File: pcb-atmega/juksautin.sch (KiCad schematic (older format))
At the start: 29 parts, among them J1 Screw_Terminal_01x09, J2 Power out, J3 USB_C_Receptacle_USB2.0, J4 TagConnect, J5 EXTRA, J6 AREF_OUT, U1 SP3485EN, U2 SRV05-4, U3 R-78E5.0-0.5, U4 ATmega32U4-AU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

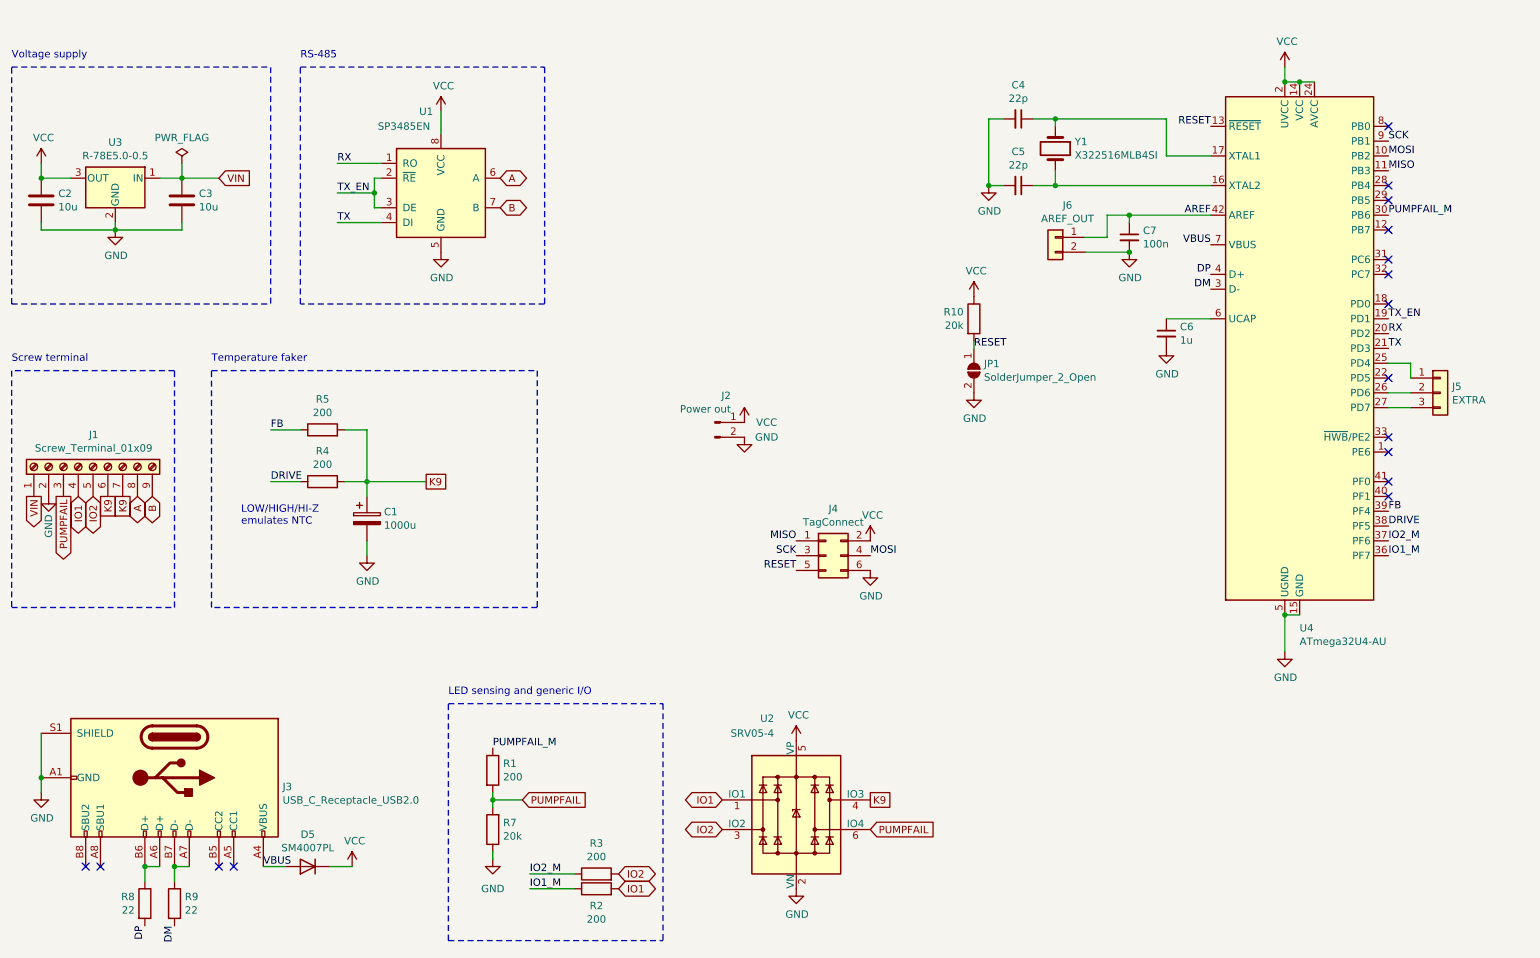
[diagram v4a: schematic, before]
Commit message: Atmega328 based pcb layed out
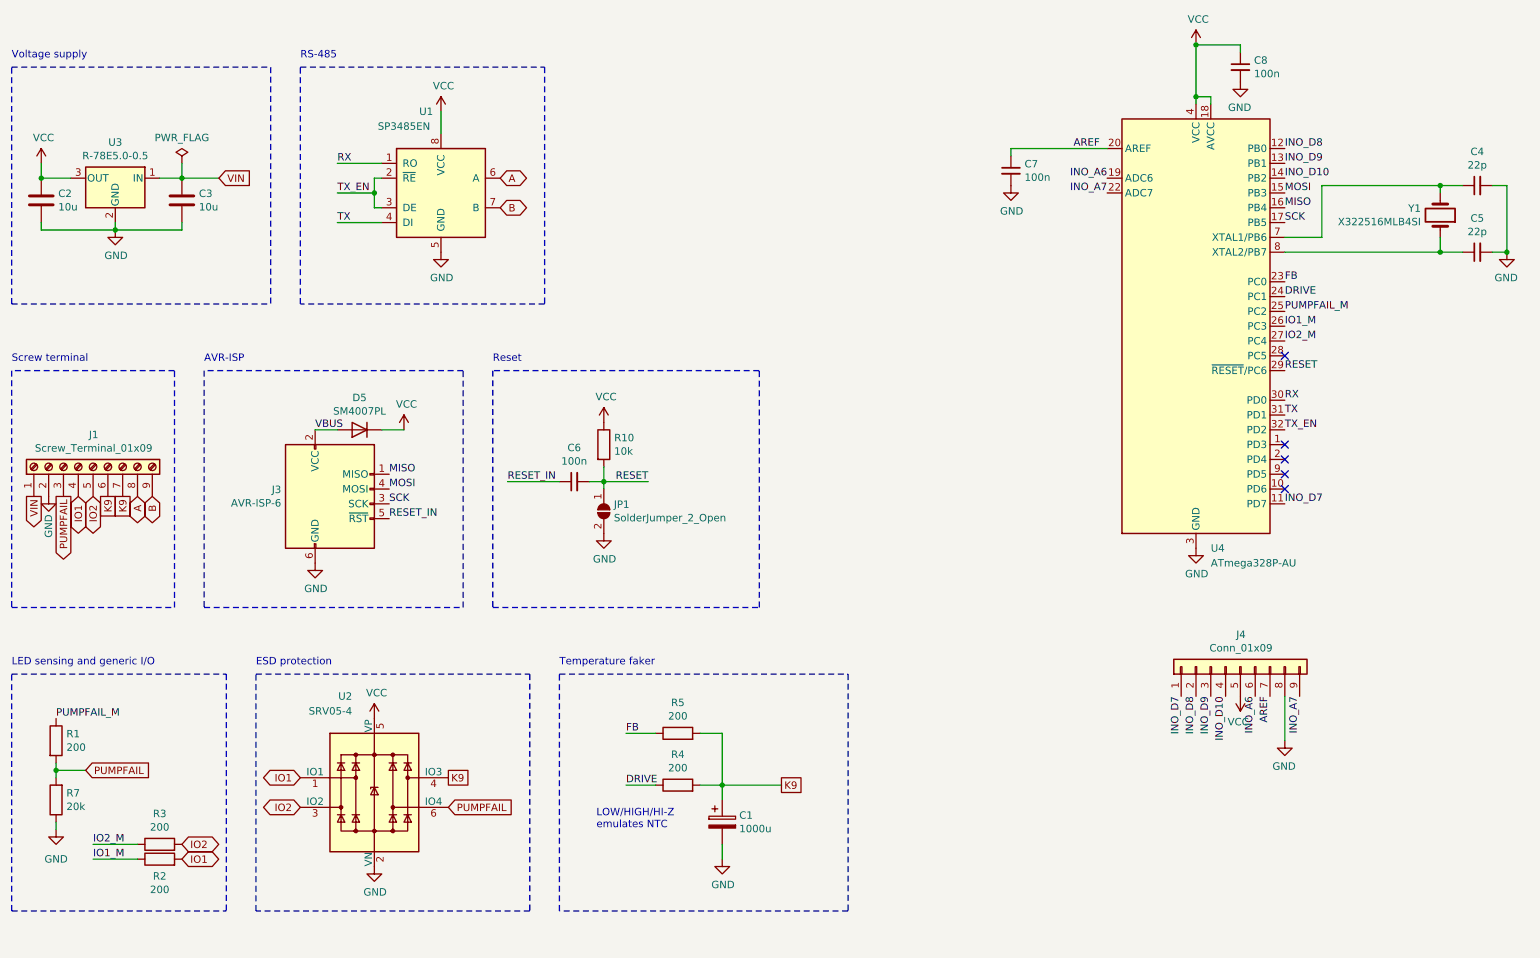
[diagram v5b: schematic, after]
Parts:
- removed J2: Power out, Connector_PinHeader_2.54mm:PinHeader_1x02_P2.54mm_Vertical, symbol Connector:Conn_01x02_Male
- removed J3: USB_C_Receptacle_USB2.0, Connector_USB:USB_C_Receptacle_HRO_TYPE-C-31-M-12, symbol Connector:USB_C_Receptacle_USB2.0
- removed J4: TagConnect, Connector:Tag-Connect_TC2030-IDC-NL_2x03_P1.27mm_Vertical, symbol Connector_Generic:Conn_02x03_Odd_Even
- removed J5: EXTRA, Connector_PinHeader_2.54mm:PinHeader_1x03_P2.54mm_Vertical, symbol Connector_Generic:Conn_01x03
- removed J6: AREF_OUT, Connector_PinHeader_2.54mm:PinHeader_1x02_P2.54mm_Vertical, symbol Connector_Generic:Conn_01x02
- removed R8, R9: 22, Resistor_SMD:R_0603_1608Metric, symbol Device:R
- removed U4: ATmega32U4-AU, Package_QFP:TQFP-44_10x10mm_P0.8mm, symbol MCU_Microchip_ATmega:ATmega32U4-AU
- added C8: 100n, Capacitor_SMD:C_0402_1005Metric, symbol Device:C_Small
- added J3: AVR-ISP-6, Connector_IDC:IDC-Header_2x03_P2.54mm_Horizontal, symbol Connector:AVR-ISP-6
- added J4: Conn_01x09, Connector_PinHeader_2.54mm:PinHeader_1x09_P2.54mm_Vertical, symbol Connector_Generic:Conn_01x09
- added U4: ATmega328P-AU, Package_QFP:TQFP-32_7x7mm_P0.8mm, symbol MCU_Microchip_ATmega:ATmega328P-AU
- C6: value 1u -> 100n; LCSC C52923 -> C1525
- R10: value 20k -> 10k; LCSC C4184 -> C25804
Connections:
- net AREF: now also J4.7 (Pin_7), U4.20 (AREF)
- net DRIVE: now also U4.24 (PC1)
- net FB: now also U4.23 (PC0)
- net GND: now also C8.2, J3.6 (GND), J4.8 (Pin_8), U4.21 (GND), U4.3 (GND), U4.5 (GND); no longer C6.2
- net IO1_M: now also U4.26 (PC3)
- net IO2_M: now also U4.27 (PC4)
- net MISO: now also J3.1 (MISO), U4.16 (PB4)
- net MOSI: now also J3.4 (MOSI), U4.15 (PB3)
- net PUMPFAIL_M: now also U4.25 (PC2)
- net RESET: now also C6.2, U4.29 (~RESET~/PC6)
- net RX: now also U4.30 (PD0)
- net SCK: now also J3.3 (SCK), U4.17 (PB5)
- net TX: now also U4.31 (PD1)
- net TX_EN: now also U4.32 (PD2)
- net VBUS: now also J3.2 (VCC)
- net VCC: now also C8.1, J4.5 (Pin_5), U4.18 (AVCC), U4.4 (VCC), U4.6 (VCC)
- net at C5.1: now also Y1.1, U4.8 (XTAL2/PB7); no longer Y1.2
- net at C4.1: now also Y1.2, U4.7 (XTAL1/PB6); no longer Y1.1
- net RESET_IN: now reaches C6.1
- net RESET_IN: now also J3.5 (~RST)
- new net INO_A6: J4.6 (Pin_6), U4.19 (ADC6)
- new net INO_A7: J4.9 (Pin_9), U4.22 (ADC7)
- new net INO_D10: J4.4 (Pin_4), U4.14 (PB2)
- new net INO_D7: J4.1 (Pin_1), U4.11 (PD7)
- new net INO_D8: J4.2 (Pin_2), U4.12 (PB0)
- new net INO_D9: J4.3 (Pin_3), U4.13 (PB1)
- no-connect marks 16 -> 5
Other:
- note added: "AVR-ISP"
- note added: "ESD protection"
- note added: "Reset"
- moved on the sheet: C1, C4, C5, C7, D5, JP1, R1, R10, R2, R3, R4, R5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

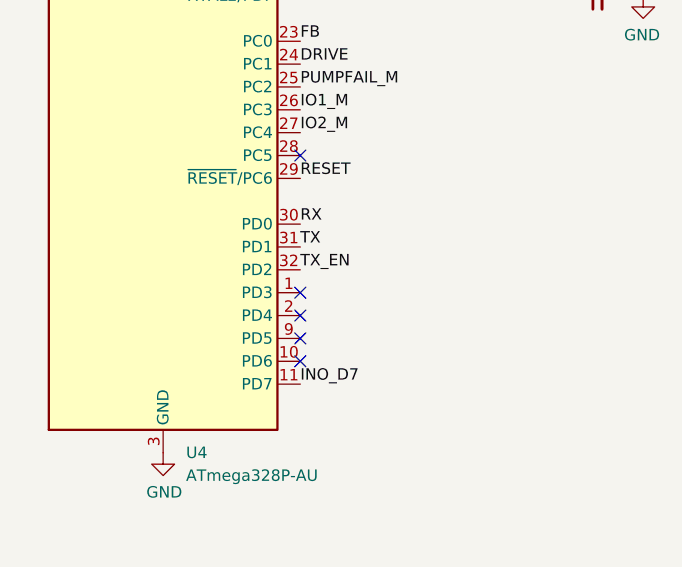
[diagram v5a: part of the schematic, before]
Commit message: Add an indicator LED
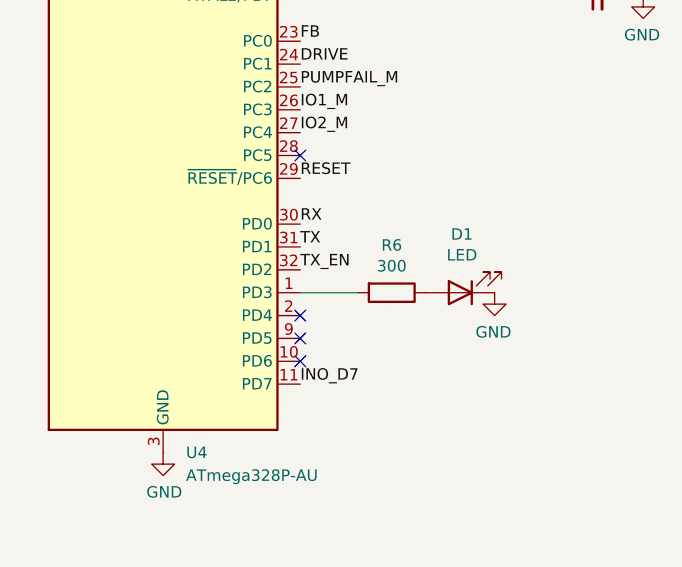
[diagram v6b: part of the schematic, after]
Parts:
- added D1: LED, LED_SMD:LED_0603_1608Metric, symbol Device:LED
- added R6: 300, Resistor_SMD:R_0603_1608Metric, symbol Device:R
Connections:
- net GND: now also D1.1 (K)
- net at U4.1 (PD3): now also R6.2
- new net: D1.2 (A), R6.1
- no-connect marks 5 -> 4
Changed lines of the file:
@@
 	0    -1   1    0
 $EndComp
-Connection ~ 10950 2250
 Wire Wire Line
 	10950 1800 10950 2250
@@
 L power:GND #PWR02
 U 1 1 60B9E570
-P 10950 2250
-F 0 "#PWR02" H 10950 2000 50  0001 C CNN
-F 1 "GND" H 10955 2077 50  0000 C CNN
-F 2 "" H 10950 2250 50  0001 C CNN
-F 3 "" H 10950 2250 50  0001 C CNN
-	1    10950 2250
+P 10300 3550
+F 0 "#PWR02" H 10300 3300 50  0001 C CNN
+F 1 "GND" H 10305 3377 50  0000 C CNN
+F 2 "" H 10300 3550 50  0001 C CNN
+F 3 "" H 10300 3550 50  0001 C CNN
+	1    10300 3550
 	-1   0    0    -1
 $EndComp
@@
 NoConn ~ 9450 2950
 NoConn ~ 9450 3850
-NoConn ~ 9450 3550
 Wire Wire Line
 	10500 1800 9700 1800
@@
 Text Label 9450 3950 0    50   ~ 0
 INO_D7
+$Comp
+L Device:LED D1
+U 1 1 61105A7E
+P 10150 3550
+F 0 "D1" H 10143 3295 50  0000 C CNN
+F 1 "LED" H 10143 3386 50  0000 C CNN
+F 2 "LED_SMD:LED_0603_1608Metric" H 10150 3550 50  0001 C CNN
+F 3 "~" H 10150 3550 50  0001 C CNN
+F 4 "C72043" H 10150 3550 50  0001 C CNN "LCSC"
+	1    10150 3550
+	-1   0    0    1
+$EndComp
+$Comp
+L Device:R R6
+U 1 1 611065FB
+P 9850 3550
+F 0 "R6" V 9643 3550 50  0000 C CNN
+F 1 "300" V 9734 3550 50  0000 C CNN
+F 2 "Resistor_SMD:R_0603_1608Metric" V 9780 3550 50  0001 C CNN
+F 3 "~" H 9850 3550 50  0001 C CNN
+F 4 "C23025" V 9850 3550 50  0001 C CNN "LCSC"
+	1    9850 3550
+	0    1    1    0
+$EndComp
+Wire Wire Line
+	9450 3550 9700 3550
+$Comp
+L power:GND #PWR?
+U 1 1 6111F566
+P 10950 2250
+F 0 "#PWR?" H 10950 2000 50  0001 C CNN
+F 1 "GND" H 10955 2077 50  0000 C CNN
+F 2 "" H 10950 2250 50  0001 C CNN
+F 3 "" H 10950 2250 50  0001 C CNN
+	1    10950 2250
+	-1   0    0    -1
+$EndComp
+Connection ~ 10950 2250
 $EndSCHEMATC

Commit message: pcb: Replace IDC-6 connector with plain pins. The casing is 3D printed.
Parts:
- J3: footprint Connector_IDC:IDC-Header_2x03_P2.54mm_Horizontal -> Connector_PinHeader_2.54mm:PinHeader_2x03_P2.54mm_Horizontal
- JP1: value SolderJumper_2_Open -> Reset pad
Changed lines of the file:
@@
 P 4850 4000
 F 0 "JP1" V 4804 4068 50  0000 L CNN
-F 1 "SolderJumper_2_Open" V 4895 4068 50  0000 L CNN
+F 1 "Reset pad" V 4895 4068 50  0000 L CNN
 F 2 "Jumper:SolderJumper-2_P1.3mm_Open_Pad1.0x1.5mm" H 4850 4000 50  0001 C CNN
 F 3 "~" H 4850 4000 50  0001 C CNN
@@
 F 0 "J3" H 2671 4046 50  0000 R CNN
 F 1 "AVR-ISP-6" H 2671 3955 50  0000 R CNN
-F 2 "Connector_IDC:IDC-Header_2x03_P2.54mm_Horizontal" V 2750 4000 50  0001 C CNN
+F 2 "Connector_PinHeader_2.54mm:PinHeader_2x03_P2.54mm_Horizontal" V 2750 4000 50  0001 C CNN
 F 3 " ~" H 1725 3400 50  0001 C CNN
 	1    3000 3950
@@
 	9450 3550 9700 3550
 $Comp
-L power:GND #PWR?
+L power:GND #PWR0106
 U 1 1 6111F566
 P 10950 2250
-F 0 "#PWR?" H 10950 2000 50  0001 C CNN
+F 0 "#PWR0106" H 10950 2000 50  0001 C CNN
 F 1 "GND" H 10955 2077 50  0000 C CNN
 F 2 "" H 10950 2250 50  0001 C CNN

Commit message: Schema and layout fixes after v0.9
- Crystal Y1 symbol changed to 4-pin, affecting the wiring as well
- Remove DC block capacitor C6, blocked RESET signal
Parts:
- removed C6: 100n, Capacitor_SMD:C_0402_1005Metric, symbol Device:C_Small
- removed Y1: X322516MLB4SI, Crystal:Crystal_SMD_3225-4Pin_3.2x2.5mm, symbol Device:Crystal
- added Y1: X322516MLB4SI, Crystal:Crystal_SMD_3225-4Pin_3.2x2.5mm, symbol Device:Crystal_GND24
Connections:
- net RESET_IN is gone; now on net RESET: J3.5 (~RST)
- net GND: now also Y1.2, Y1.4
- net at C5.1, U4.8 (XTAL2/PB7): now also Y1.1
- net at C4.1, U4.7 (XTAL1/PB6): now also Y1.3
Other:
- moved on the sheet: C4, C5
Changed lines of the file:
@@
 Wire Wire Line
 	4850 3800 4850 3700
-Text Label 4200 3800 0    50   ~ 0
-RESET_IN
 Text Label 9450 1850 0    50   ~ 0
 MOSI
@@
 	1    0    0    -1
 $EndComp
-Wire Wire Line
-	10850 1800 10950 1800
 $Comp
 L Device:C_Small C4
 U 1 1 60B5C443
-P 10750 1800
-F 0 "C4" V 10521 1800 50  0000 C CNN
-F 1 "22p" V 10612 1800 50  0000 C CNN
-F 2 "Capacitor_SMD:C_0402_1005Metric" H 10750 1800 50  0001 C CNN
-F 3 "~" H 10750 1800 50  0001 C CNN
-F 4 "C1555" V 10750 1800 50  0001 C CNN "LCSC"
-	1    10750 1800
-	0    -1   1    0
-$EndComp
-Wire Wire Line
-	10950 1800 10950 2250
+P 10600 2750
+F 0 "C4" V 10371 2750 50  0000 C CNN
+F 1 "22p" V 10462 2750 50  0000 C CNN
+F 2 "Capacitor_SMD:C_0402_1005Metric" H 10600 2750 50  0001 C CNN
+F 3 "~" H 10600 2750 50  0001 C CNN
+F 4 "C1555" V 10600 2750 50  0001 C CNN "LCSC"
+	1    10600 2750
+	-1   0    0    -1
+$EndComp
 $Comp
 L power:GND #PWR02
@@
 	-1   0    0    -1
 $EndComp
-Wire Wire Line
-	10850 2250 10950 2250
 $Comp
 L Device:C_Small C5
 U 1 1 60B5D62C
-P 10750 2250
-F 0 "C5" V 10521 2250 50  0000 C CNN
-F 1 "22p" V 10612 2250 50  0000 C CNN
-F 2 "Capacitor_SMD:C_0402_1005Metric" H 10750 2250 50  0001 C CNN
-F 3 "~" H 10750 2250 50  0001 C CNN
-F 4 "C1555" V 10750 2250 50  0001 C CNN "LCSC"
-	1    10750 2250
-	0    -1   1    0
+P 10200 2750
+F 0 "C5" V 9971 2750 50  0000 C CNN
+F 1 "22p" V 10062 2750 50  0000 C CNN
+F 2 "Capacitor_SMD:C_0402_1005Metric" H 10200 2750 50  0001 C CNN
+F 3 "~" H 10200 2750 50  0001 C CNN
+F 4 "C1555" V 10200 2750 50  0001 C CNN "LCSC"
+	1    10200 2750
+	-1   0    0    -1
 $EndComp
 $Comp
@@
 $EndComp
 Wire Wire Line
-	9450 2150 9700 2150
-Wire Wire Line
-	9700 2150 9700 1800
-Wire Wire Line
 	7600 1550 8250 1550
 Wire Wire Line
@@
 	9150 850  8850 850
 Connection ~ 8850 850
-$Comp
-L Device:C_Small C6
-U 1 1 60DBB221
-P 4650 3800
-F 0 "C6" V 4879 3800 50  0000 C CNN
-F 1 "100n" V 4788 3800 50  0000 C CNN
-F 2 "Capacitor_SMD:C_0402_1005Metric" H 4650 3800 50  0001 C CNN
-F 3 "~" H 4650 3800 50  0001 C CNN
-F 4 "C1525" H 4650 3800 50  0001 C CNN "LCSC"
-	1    4650 3800
-	0    -1   -1   0
-$EndComp
-Wire Wire Line
-	4750 3800 4850 3800
 Connection ~ 4850 3800
-Wire Wire Line
-	4550 3800 4200 3800
 Text Label 5150 3800 2    50   ~ 0
 RESET
@@
 	4850 3800 5150 3800
 Text Label 3400 4050 0    50   ~ 0
-RESET_IN
+RESET
 Wire Wire Line
 	4850 3850 4850 3800
@@
 NoConn ~ 9450 2950
 NoConn ~ 9450 3850
-Wire Wire Line
-	10500 1800 9700 1800
-Connection ~ 10500 1800
-Wire Wire Line
-	10650 1800 10500 1800
-Wire Wire Line
-	10500 2250 9450 2250
-Connection ~ 10500 2250
-Wire Wire Line
-	10650 2250 10500 2250
-Wire Wire Line
-	10500 2150 10500 2250
-Wire Wire Line
-	10500 1800 10500 1850
-$Comp
-L Device:Crystal Y1
-U 1 1 60B59932
-P 10500 2000
-F 0 "Y1" V 10546 1869 50  0000 R CNN
-F 1 "X322516MLB4SI" V 10455 1869 50  0000 R CNN
-F 2 "Crystal:Crystal_SMD_3225-4Pin_3.2x2.5mm" H 10500 2000 50  0001 C CNN
-F 3 "~" H 10500 2000 50  0001 C CNN
-F 4 "C13738" V 10500 2000 50  0001 C CNN "LCSC"
-	1    10500 2000
-	0    1    -1   0
-$EndComp
 Text Notes 2500 5050 0    50   ~ 0
 ESD protection
@@
 L power:GND #PWR0106
 U 1 1 6111F566
-P 10950 2250
-F 0 "#PWR0106" H 10950 2000 50  0001 C CNN
-F 1 "GND" H 10955 2077 50  0000 C CNN
-F 2 "" H 10950 2250 50  0001 C CNN
-F 3 "" H 10950 2250 50  0001 C CNN
-	1    10950 2250
+P 11000 2900
+F 0 "#PWR0106" H 11000 2650 50  0001 C CNN
+F 1 "GND" H 11005 2727 50  0000 C CNN
+F 2 "" H 11000 2900 50  0001 C CNN
+F 3 "" H 11000 2900 50  0001 C CNN
+	1    11000 2900
 	-1   0    0    -1
 $EndComp
-Connection ~ 10950 2250
+$Comp
+L Device:Crystal_GND24 Y1
+U 1 1 60CA5FA0
+P 10400 2400
+F 0 "Y1" V 10350 2700 50  0000 L CNN
+F 1 "X322516MLB4SI" V 10450 2700 50  0000 L CNN
+F 2 "Crystal:Crystal_SMD_3225-4Pin_3.2x2.5mm" H 10400 2400 50  0001 C CNN
+F 3 "~" H 10400 2400 50  0001 C CNN
+	1    10400 2400
+	1    0    0    -1
+$EndComp
+Wire Wire Line
+	10600 2400 10600 2150
+Wire Wire Line
+	9450 2150 10600 2150
+Wire Wire Line
+	10550 2400 10600 2400
+Connection ~ 10600 2400
+Wire Wire Line
+	10600 2400 10600 2650
+Wire Wire Line
+	10250 2400 10200 2400
+Wire Wire Line
+	10200 2400 10200 2650
+Wire Wire Line
+	9450 2250 10200 2250
+Wire Wire Line
+	10200 2250 10200 2400
+Connection ~ 10200 2400
+Wire Wire Line
+	10400 2600 11000 2600
+Wire Wire Line
+	11000 2600 11000 2200
+Wire Wire Line
+	11000 2200 10400 2200
+Connection ~ 11000 2600
+Wire Wire Line
+	11000 2900 10600 2900
+Wire Wire Line
+	10200 2900 10200 2850
+Connection ~ 11000 2900
+Wire Wire Line
+	11000 2600 11000 2900
+Wire Wire Line
+	10600 2900 10600 2850
+Connection ~ 10600 2900
+Wire Wire Line
+	10600 2900 10200 2900
 $EndSCHEMATC
